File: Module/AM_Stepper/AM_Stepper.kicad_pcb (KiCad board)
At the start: 2 copper layers, 20.4 x 30.6 mm, 6 parts, among them J1 CONN_01X04, J2 CONN_01X04, J3 CONN_01X03, M1 Aktuator_Module

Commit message: Added outputs, pdf, screenshots
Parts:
- added G***: LOGO, Hardware:EP_Logo_3, B.Cu at (160.6, 87.7)
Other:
- board text added: "1"
- board text added: "1->1B;1A;2B;2A;"

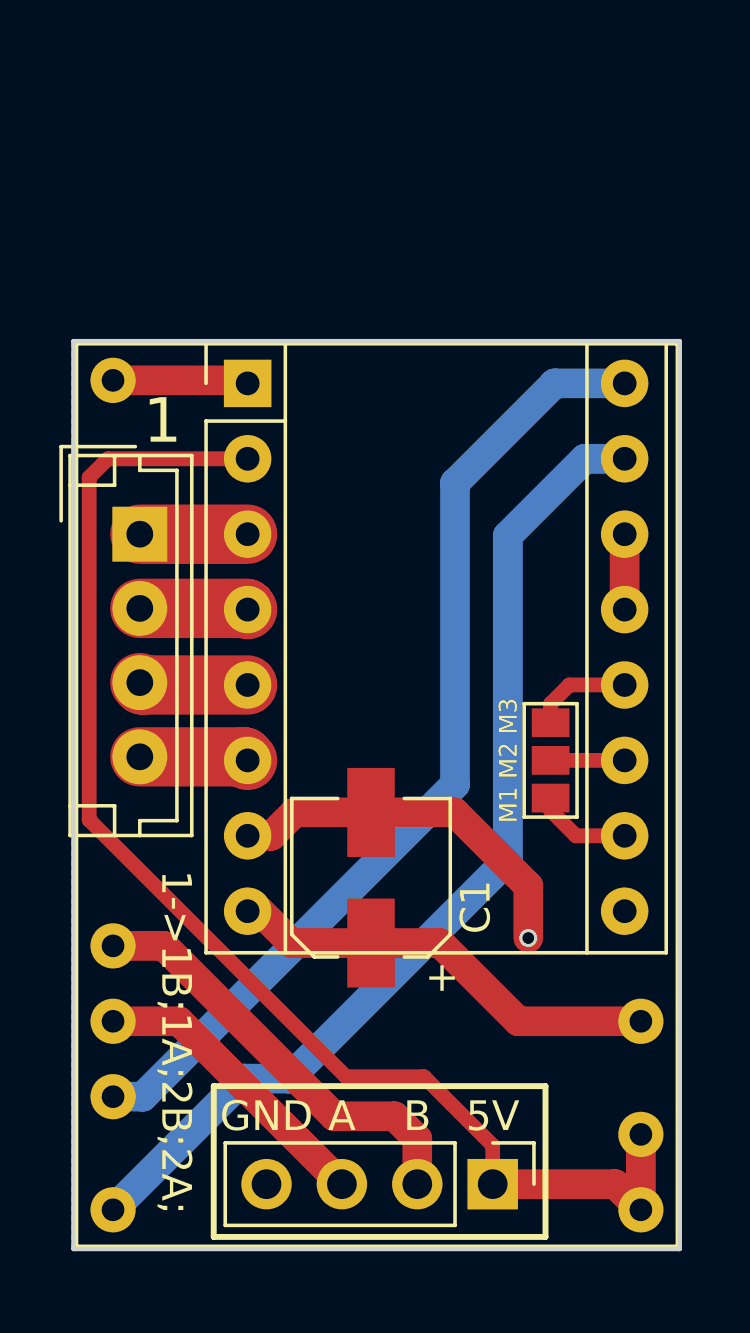
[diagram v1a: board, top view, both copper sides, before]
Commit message: Extending the stepper and redesigning
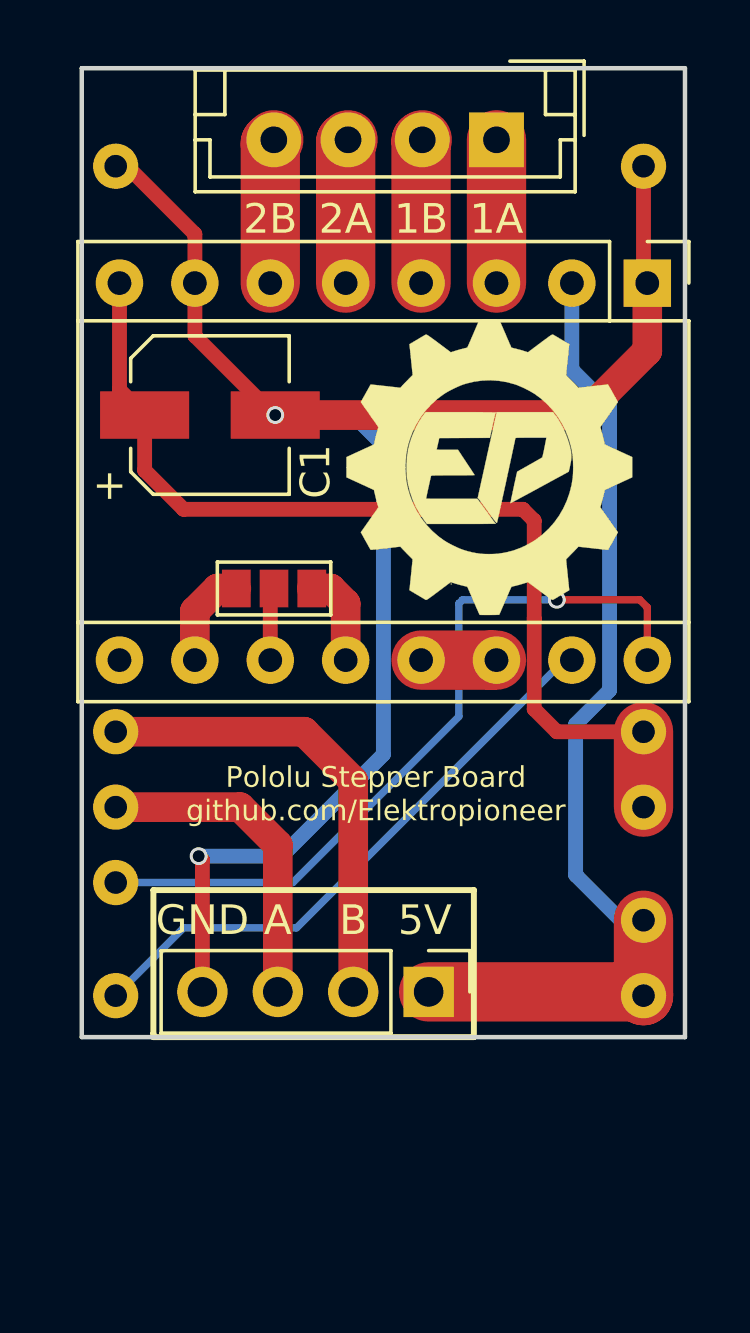
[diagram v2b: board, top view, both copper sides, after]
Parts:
- G***: moved to F.Cu
- moved J1 17.9 mm to (162.7, 67.7), turned to 180 degrees
- moved C1 16.5 mm to (153.0, 77.0), turned to 0 degrees
- moved A1 13.9 mm to (167.8, 72.5), turned to 270 degrees
- moved J3 11.0 mm to (155.2, 82.8), turned to 270 degrees
- moved G*** 9.57 mm to (162.6, 78.4), turned to 0 degrees
- moved M1 7.21 mm to (148.6, 97.8)
- moved J2 6.83 mm to (160.4, 96.4)
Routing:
- net GND: track 17.1 -> 57.3 mm, vias 1 -> 2
- net +12V: track 14.9 -> 33.4 mm
- net STEP: track 34.1 -> 20.0 mm
- net +5V: track 44.5 -> 33.7 mm
- net DIRECTION: track 33.1 -> 26.0 mm, vias 0 -> 1
- net ENC_B: track 14.5 -> 15.8 mm
- net Net-(A1-Pad4): track 3.65 -> 4.84 mm
- net Net-(A1-Pad5): track 3.67 -> 4.86 mm
- net Net-(A1-Pad3): track 3.63 -> 4.83 mm
- net Net-(A1-Pad6): track 3.68 -> 4.88 mm
- net ENC_A: track 9.98 -> 10.9 mm
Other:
- board size 20.4 x 30.6 mm -> 20.3 x 32.6 mm
- board text added: "1A"
- board text added: "1B"
- board text added: "2A"
- board text added: "2B"
- board text added: "Pololu Stepper Board github.com/Elektropioneer"
- board text removed: "1"
- board text removed: "1->1B;1A;2B;2A;"
- board text removed: "M1 M2 M3"
- board text removed: "Pololu Stepper D. EP Module"
